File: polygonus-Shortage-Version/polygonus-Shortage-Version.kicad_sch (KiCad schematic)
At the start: 14 parts, among them J105 Conn_01x01, J107 Conn_01x01, J108 Conn_01x01, J3 Conn_01x32, J5 Conn_01x32, J6 Conn_01x16, J7 Conn_01x16

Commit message: Moved highsides about
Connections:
- net HS1: now also J7.1 (Pin_1); no longer J7.4 (Pin_4)
- net HS2: now also J7.2 (Pin_2); no longer J7.3 (Pin_3)
- net HS3: now also J7.3 (Pin_3); no longer J7.2 (Pin_2)
- net HS4: now also J7.4 (Pin_4); no longer J7.1 (Pin_1)
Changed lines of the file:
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@@
+    (effects (font (size 1.27 1.27)) (justify right bottom))
+  )
+  (label "HS1" (at 273.2114 24.1919 180)
     (effects (font (size 1.27 1.27)) (justify right bottom))
   )
@@
     (effects (font (size 1.27 1.27)) (justify right bottom))
   )
-  (label "HS2" (at 273.2114 29.2719 180)
-    (effects (font (size 1.27 1.27)) (justify right bottom))
-  )
   (label "AV9" (at 45.085 57.15 180)
     (effects (font (size 1.27 1.27)) (justify right bottom))
@@
     (effects (font (size 1.27 1.27)) (justify right bottom))
   )
+  (label "HS3" (at 273.2114 29.2719 180)
+    (effects (font (size 1.27 1.27)) (justify right bottom))
+  )
   (label "12V_PROT" (at 62.23 109.855 180)
     (effects (font (size 1.27 1.27)) (justify right bottom))
@@
     (effects (font (size 1.27 1.27)) (justify right bottom))
   )
+  (label "HS2" (at 273.2114 26.7319 180)
+    (effects (font (size 1.27 1.27)) (justify right bottom))
+  )
   (label "AT2" (at 37.465 78.105 180)
     (effects (font (size 1.27 1.27)) (justify right bottom))
@@
     (effects (font (size 1.27 1.27)) (justify right bottom))
   )
-  (label "HS1" (at 273.2114 31.8119 180)
-    (effects (font (size 1.27 1.27)) (justify right bottom))
-  )
   (label "CAN-" (at 16.51 121.92 180)
     (effects (font (size 1.27 1.27)) (justify right bottom))
@@
     (effects (font (size 1.27 1.27)) (justify left bottom))
   )
-  (label "HS3" (at 273.2114 26.7319 180)
-    (effects (font (size 1.27 1.27)) (justify right bottom))
-  )
   (label "LS12" (at 140.97 57.15 0)
     (effects (font (size 1.27 1.27)) (justify left bottom))
@@
     (effects (font (size 1.27 1.27)) (justify left bottom))
   )
-  (label "HS4" (at 273.2114 24.1919 180)
-    (effects (font (size 1.27 1.27)) (justify right bottom))
-  )
+  (label "HS4" (at 273.2114 31.8119 180)
+    (effects (font (size 1.27 1.27)) (justify right bottom))
+  )

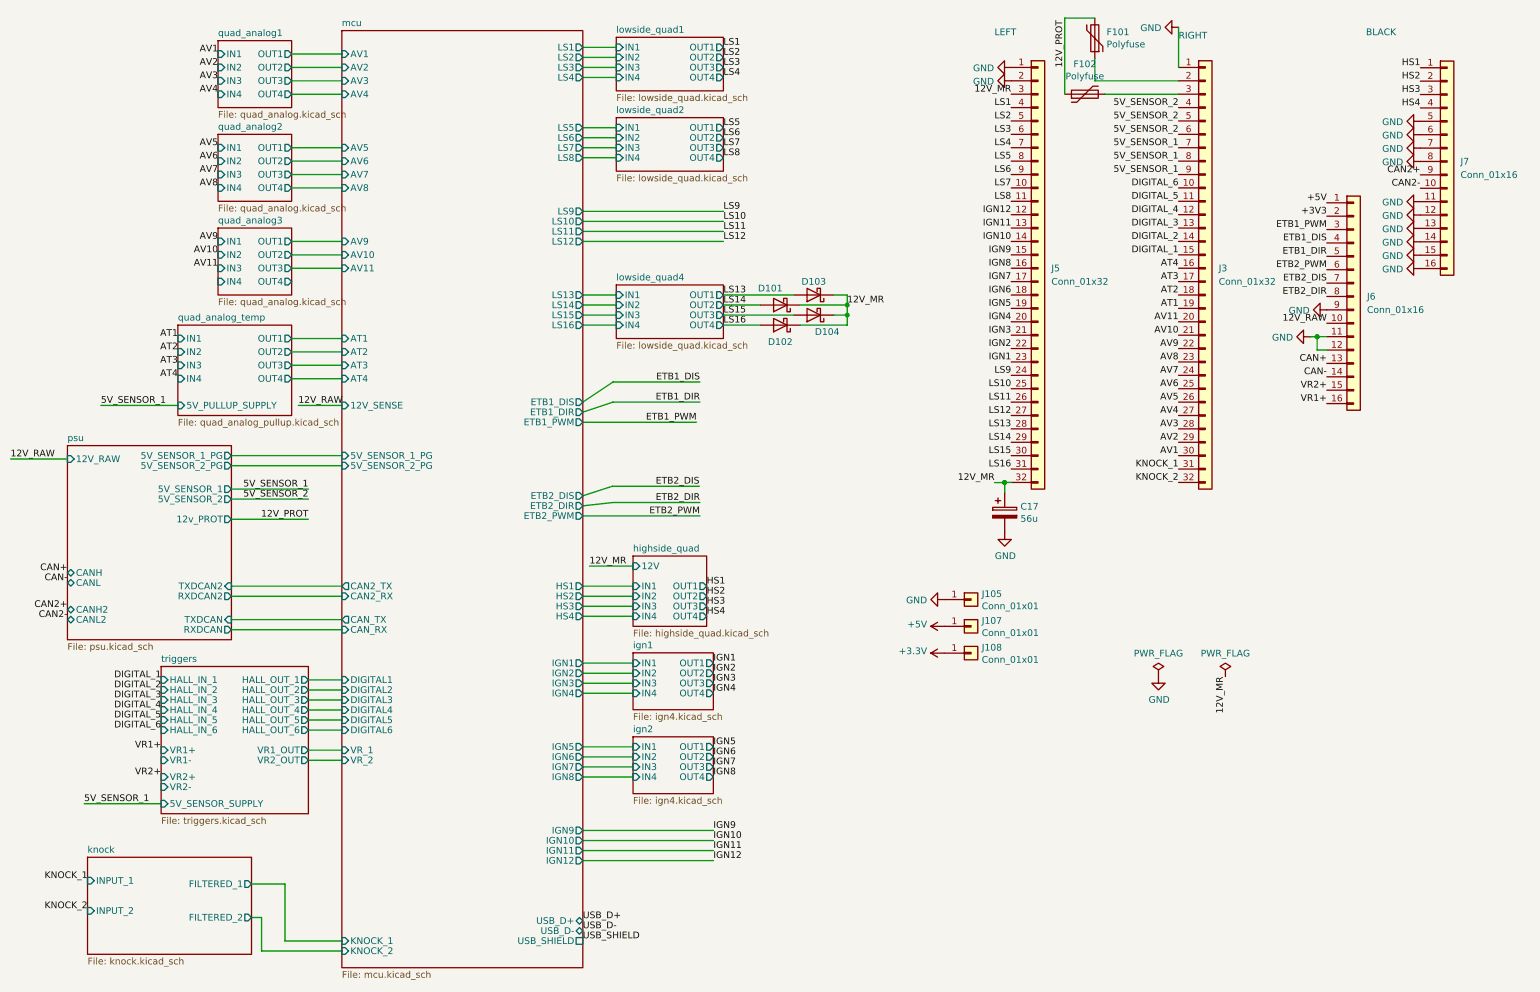
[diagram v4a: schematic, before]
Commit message: Added Keep_Alive power circuit
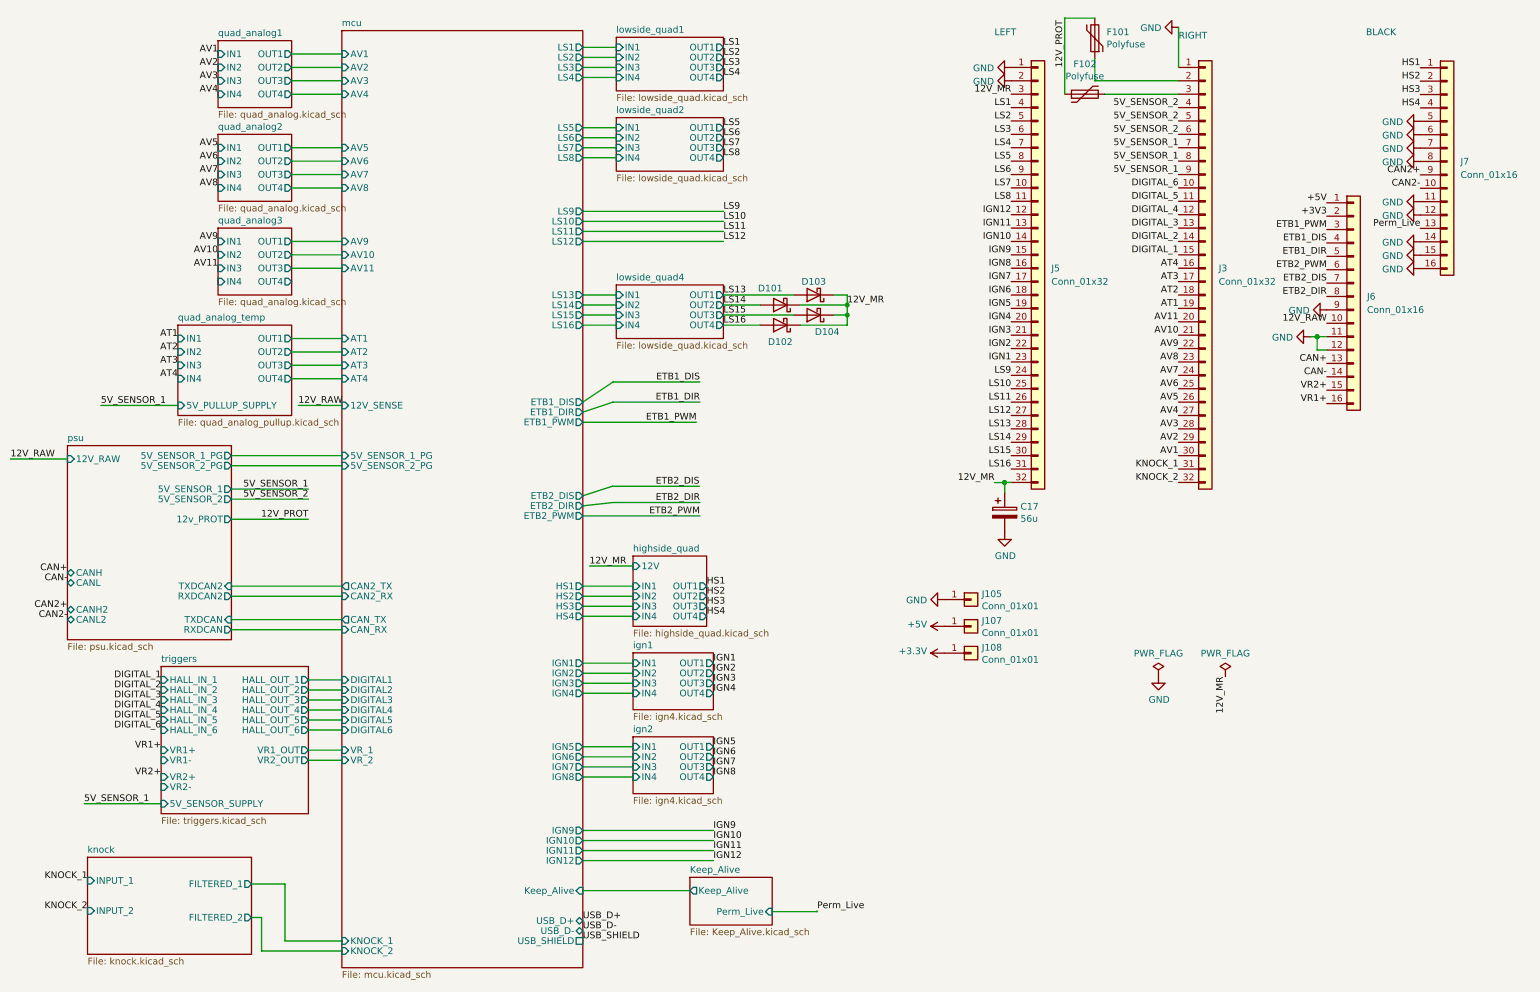
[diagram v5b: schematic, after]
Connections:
- net GND: no longer J7.13 (Pin_13)
- new net Perm_Live: J7.13 (Pin_13)
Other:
- added sheet Keep_Alive (Keep_Alive.kicad_sch)
- sheet mcu ports: added Keep_Alive; removed none
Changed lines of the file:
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@@
     (stroke (width 0) (type default) (color 0 0 0 0))
   )
+  (wire (pts (xy 150.2316 184.3116) (xy 158.75 184.3116))
+    (stroke (width 0) (type default) (color 0 0 0 0))
+  )
   (wire (pts (xy 114.3 168.91) (xy 139.065 168.91))
     (stroke (width 0) (type default) (color 0 0 0 0))
@@
     (stroke (width 0) (type default) (color 0 0 0 0))
   )
+  (wire (pts (xy 114.3 180.325) (xy 114.3 180.34))
+    (stroke (width 0) (type default) (color 0 0 0 0))
+  )
   (wire (pts (xy 120.65 41.275) (xy 114.3 41.275))
     (stroke (width 0) (type default) (color 0 0 0 0))
@@
     (stroke (width 0) (type default) (color 0 0 0 0))
   )
+  (wire (pts (xy 134.62 180.325) (xy 114.3 180.325))
+    (stroke (width 0) (type default) (color 0 0 0 0))
+  )
   (wire (pts (xy 68.58 59.69) (xy 59.055 59.69))
     (stroke (width 0) (type default) (color 0 0 0 0))
@@
     (stroke (width 0) (type default) (color 0 0 0 0))
   )
+  (wire (pts (xy 158.75 184.3116) (xy 158.75 184.15))
+    (stroke (width 0) (type default) (color 0 0 0 0))
+  )
   (wire (pts (xy 59.055 62.23) (xy 68.58 62.23))
     (stroke (width 0) (type default) (color 0 0 0 0))
@@
     (effects (font (size 1.27 1.27)) (justify right bottom))
   )
+  (label "Perm_Live" (at 158.75 184.15 0)
+    (effects (font (size 1.27 1.27)) (justify left bottom))
+  )
   (label "AV9" (at 45.085 57.15 180)
     (effects (font (size 1.27 1.27)) (justify right bottom))
@@
     (effects (font (size 1.27 1.27)) (justify left bottom))
   )
+  (label "Perm_Live" (at 273.2114 54.6719 180)
+    (effects (font (size 1.27 1.27)) (justify right bottom))
+  )
   (label "12V_RAW" (at 255.4645 72.6696 180)
     (effects (font (size 1.27 1.27)) (justify right bottom))
@@
     (pin "1")
   )
-  (symbol (lib_id "power:GND") (at 273.2114 54.6719 270) (unit 1)
-    (in_bom yes) (on_board yes)
-    (property "Reference" "#PWR0147" (id 0) (at 266.8614 54.6719 0)
-      (effects (font (size 1.27 1.27)) hide)
-    )
-    (property "Value" "GND" (id 1) (at 269.9602 54.7989 90)
-      (effects (font (size 1.27 1.27)) (justify right))
-    )
-    (property "Footprint" "" (id 2) (at 273.2114 54.6719 0)
-      (effects (font (size 1.27 1.27)) hide)
-    )
-    (property "Datasheet" "" (id 3) (at 273.2114 54.6719 0)
-      (effects (font (size 1.27 1.27)) hide)
-    )
-    (pin "1")
-  )
   (symbol (lib_id "Connector_Generic:Conn_01x32") (at 232.41 62.23 0) (unit 1)
     (in_bom yes) (on_board yes) (fields_autoplaced)
@@
       (effects (font (size 1.27 1.27)) (justify left))
     )
+    (pin "Keep_Alive" input (at 114.3 180.34 0)
+      (effects (font (size 1.27 1.27)) (justify right))
+    )
   )
   (sheet (at 120.65 33.655) (size 20.32 10.16) (fields_autoplaced)
@@
     )
   )
+  (sheet (at 134.62 177.8) (size 15.6116 9.047) (fields_autoplaced)
+    (stroke (width 0.1524) (type solid) (color 0 0 0 0))
+    (fill (color 0 0 0 0.0000))
+    (property "Sheet name" "Keep_Alive" (id 0) (at 134.62 177.0884 0)
+      (effects (font (size 1.27 1.27)) (justify left bottom))
+    )
+    (property "Sheet file" "Keep_Alive.kicad_sch" (id 1) (at 134.62 187.4316 0)
+      (effects (font (size 1.27 1.27)) (justify left top))
+    )
+    (pin "Perm_Live" input (at 150.2316 184.3116 0)
+      (effects (font (size 1.27 1.27)) (justify right))
+    )
+    (pin "Keep_Alive" output (at 134.62 180.325 180)
+      (effects (font (size 1.27 1.27)) (justify left))
+    )
+  )
   (sheet_instances
     (path "/" (page "1"))
@@
     (path "/00000000-0000-0000-0000-00005d99f54c" (page "13"))
     (path "/00000000-0000-0000-0000-00005dd5b2e0" (page "16"))
+    (path "/46495fed-359e-4c30-808a-9217af090de7" (page "16"))
     (path "/00000000-0000-0000-0000-00005d975f3c" (page "17"))
     (path "/00000000-0000-0000-0000-00005d98f734" (page "18"))
@@
       (reference "#PWR05") (unit 1) (value "+3.3V") (footprint "")
     )
+    (path "/46495fed-359e-4c30-808a-9217af090de7/4b418118-9a44-46bd-bbf9-b8dd607fa509"
+      (reference "#PWR06") (unit 1) (value "GND") (footprint "")
+    )
+    (path "/46495fed-359e-4c30-808a-9217af090de7/15670d25-71e9-492e-8345-cd5b8996a9d1"
+      (reference "#PWR07") (unit 1) (value "GND") (footprint "")
+    )
+    (path "/46495fed-359e-4c30-808a-9217af090de7/7b5d742b-78f7-4bea-b8b4-30c6d50c51bd"
+      (reference "#PWR08") (unit 1) (value "GND") (footprint "")
+    )
+    (path "/46495fed-359e-4c30-808a-9217af090de7/339986c8-4087-467c-b1cc-d915413f866c"
+      (reference "#PWR09") (unit 1) (value "GND") (footprint "")
+    )
     (path "/00000000-0000-0000-0000-00005d9e3ba1"
       (reference "#PWR0101") (unit 1) (value "GND") (footprint "")
@@
       (reference "#PWR0146") (unit 1) (value "GND") (footprint "")
     )
-    (path "/8da41e7d-3eab-4c62-8aeb-bb291561fe7c"
-      (reference "#PWR0147") (unit 1) (value "GND") (footprint "")
-    )
     (path "/00000000-0000-0000-0000-00005d98a146/85b0c444-48f2-41ee-b642-b6821afa6059"
       (reference "#PWR0148") (unit 1) (value "GND") (footprint "")
@@
       (reference "C31") (unit 1) (value "1n") (footprint "Capacitor_SMD:C_0603_1608Metric")
     )
+    (path "/46495fed-359e-4c30-808a-9217af090de7/bb6eb5d1-10bf-4639-a353-af96ffdf880d"
+      (reference "C32") (unit 1) (value "100n") (footprint "Capacitor_SMD:C_0201_0603Metric")
+    )
+    (path "/46495fed-359e-4c30-808a-9217af090de7/5cbc2301-d77c-4265-840f-ffcb5df50b22"
+      (reference "C33") (unit 1) (value "4.7u") (footprint "Capacitor_SMD:C_0201_0603Metric")
+    )
     (path "/00000000-0000-0000-0000-00005d9a3845/00000000-0000-0000-0000-00005dd4ee13"
       (reference "C701") (unit 1) (value "100n") (footprint "Capacitor_SMD:C_0603_1608Metric")
@@
       (reference "D4") (unit 1) (value "schottky") (footprint "Diode_SMD:D_SOD-123")
     )
+    (path "/46495fed-359e-4c30-808a-9217af090de7/db2f74b5-3a9b-454b-a453-16421c0f8cc3"
+      (reference "D5") (unit 1) (value "1N4148WS") (footprint "Diode_SMD:D_SOD-323")
+    )
+    (path "/46495fed-359e-4c30-808a-9217af090de7/66496a83-8028-4c5c-a7e0-e19b4586ca05"
+      (reference "D6") (unit 1) (value "1N4148WS") (footprint "Diode_SMD:D_SOD-323")
+    )
     (path "/00000000-0000-0000-0000-00005e988fe1"
       (reference "D101") (unit 1) (value "D_Schottky") (footprint "Diode_SMD:D_SMA")
@@
       (reference "FB1501") (unit 1) (value "Ferrite_Bead") (footprint "Inductor_SMD:L_0805_2012Metric")
     )
+    (path "/46495fed-359e-4c30-808a-9217af090de7/0651f4fd-d08f-43bb-8a38-8e41030a25da"
+      (reference "IC1") (unit 1) (value "PSM712-LF-T7") (footprint "Package_TO_SOT_SMD:SOT-23")
+    )
     (path "/00000000-0000-0000-0000-00005d99e6ee/00000000-0000-0000-0000-00005f3076e2"
       (reference "J1") (unit 1) (value "Micro_SD_Card") (footprint "Connector_Card:microSD_HC_Wuerth_693072010801")
@@
       (reference "R53") (unit 1) (value "2.7k") (footprint "Resistor_SMD:R_0603_1608Metric")
     )
+    (path "/46495fed-359e-4c30-808a-9217af090de7/b4f450ab-b735-476c-8f93-e4551a5b7880"
+      (reference "R54") (unit 1) (value "6.8k") (footprint "Resistor_SMD:R_0402_1005Metric")
+    )
     (path "/00000000-0000-0000-0000-00005d9a3845/00000000-0000-0000-0000-00005dd4ee12"
       (reference "R701") (unit 1) (value "470k") (footprint "Resistor_SMD:R_0402_1005Metric")
@@
       (reference "U26") (unit 2) (value "SN74LVC2G17DB") (footprint "Package_TO_SOT_SMD:SOT-23-6")
     )
+    (path "/46495fed-359e-4c30-808a-9217af090de7/16936c3a-6eac-4792-b9dd-f3acd9e159c3"
+      (reference "U27") (unit 1) (value "MIC5205-3.3YM5") (footprint "Package_TO_SOT_SMD:SOT-23-5")
+    )
     (path "/00000000-0000-0000-0000-00005d9a3845/00000000-0000-0000-0000-00005d9a3bfa"
